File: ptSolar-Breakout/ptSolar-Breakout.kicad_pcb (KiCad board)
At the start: 2 copper layers, 24.5 x 73.5 mm, 17 parts, among them J1 6 Pin Male Header, J2 Qwiic, J3 6 Pin Male Header, J4 Conn_02x04_Odd_Even, J5 Conn_01x03, J6 Barrel_Jack_Switch, Q1 MMBT3904, SW2 SW_SPST, U1 LM1085-5.0

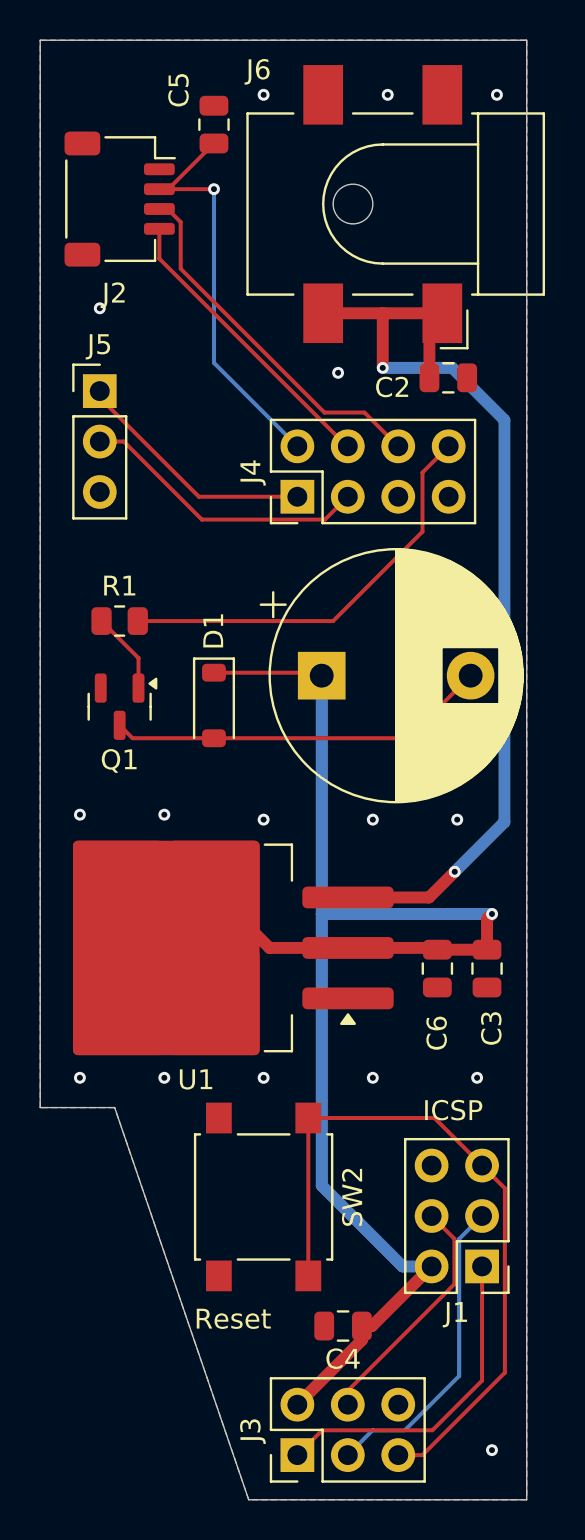
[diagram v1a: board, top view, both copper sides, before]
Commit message: Updated Breakboard to v1.1.1. Added BME280 on board. Improved silkscreening. Updated to Kicad v9.
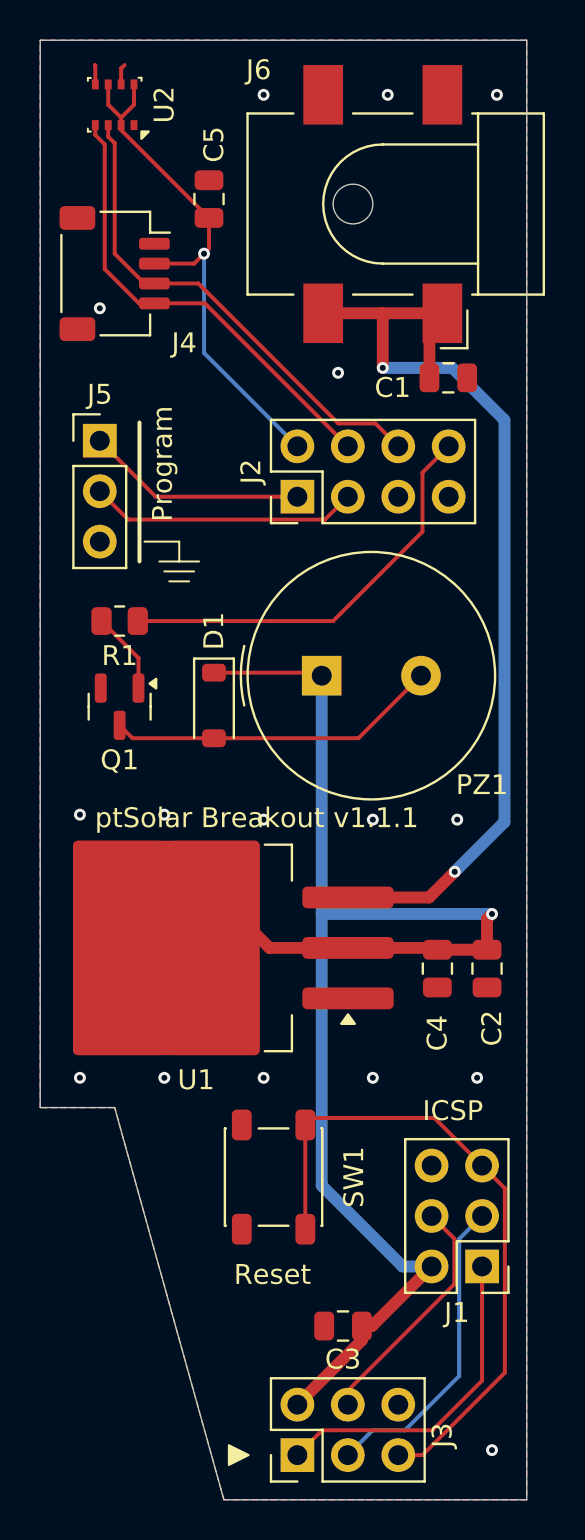
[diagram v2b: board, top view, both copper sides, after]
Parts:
- added U2: BME280, Package_LGA:Bosch_LGA-8_2.5x2.5mm_P0.65mm_ClockwisePinNumbering, F.Cu at (146.5, 71.0)
- D1: value 1N4148W -> 1N4007FL
- J1: value 6 Pin Male Header -> 6 Pin Female Socket
- J2: renamed from J4; value Conn_02x04_Odd_Even -> 8 Pin Female Socket
- J5: value Conn_01x03 -> 3 Pin Male Header
- PZ1: renamed from C1; value C -> Piezo Buzzer; footprint Capacitor_THT:CP_Radial_D12.5mm_P7.50mm -> Buzzer_Beeper:Buzzer_TDK_PS1240P02BT_D12.2mm_H6.5mm
- SW1: renamed from SW2; value SW_SPST -> Reset Switch; footprint Button_Switch_SMD:SW_SPST_B3S-1000 -> Button_Switch_SMD:SW_SPST_PTS647_Sx38
- U1: value LM1085-5.0 -> LM1086-5.0
- moved C5 3.76 mm to (151.2, 75.8)
- moved J4 3.76 mm to (146.5, 79.5)
- moved J5 2.50 mm to (145.8, 87.9)
- moved SW1 1.12 mm to (154.5, 125.0)
- turned R1 to 0 degrees
- renumbered C2 to C1, C3 to C2, C4 to C3, C6 to C4, J2 to J4
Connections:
- J2 pad 8: Net-(J4-Pin_8) -> Net-(J2-Pin_8)
- R1 pad 1: Net-(J4-Pin_8) -> Net-(Q1-B)
- R1 pad 2: Net-(Q1-B) -> Net-(J2-Pin_8)
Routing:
- net Net-(J4-Pin_8): track 21.0 -> 0.00 mm
- net Net-(J2-Pin_8): track 0.00 -> 21.0 mm
- net Net-(J2-Pin_4): track 14.9 -> 23.4 mm
- net Net-(J2-Pin_6): track 18.4 -> 24.9 mm
- net +3.3V: track 21.1 -> 27.0 mm
- net /RESET: track 35.7 -> 33.0 mm
- net Net-(D1-A): track 19.3 -> 16.8 mm
- net GND: track 0.00 -> 2.03 mm
- net Net-(J2-Pin_3): track 14.6 -> 13.6 mm
- net Net-(J2-Pin_1): track 12.3 -> 11.4 mm
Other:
- outline, holes or cut-outs redrawn
- board text added: "Program"
- board text added: "ptSolar Breakout v1.1.1"

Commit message: Updated v1.1.2 with FET switch to shut down GPS. Generated Gerbers and sent off for manufacture.
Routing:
- net GND: vias 16 -> 18
